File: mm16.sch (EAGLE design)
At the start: 57 parts, among them IC101 ATMEGA32-PU, IC102 DS1337, IC103 MAX483CPA, IC201 LTV847, IC202 LTV847, IC203 LTV847, IC204 LTV847, Q1 32,768kHz

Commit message: Werte im Schema und Bohrungen im Layout hinzugefügt
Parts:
- C1, C101, C102, C103: value 10nF -> 100nF
- R201, R202, R203, R204, R205, R206, R207, R208, R209, R210, R211, R212, R213, R214, R215, R216: value (none) -> 220kΩ
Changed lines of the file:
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@@
 <part name="D207" library="diode" deviceset="1N4148" device="-V"/>
 <part name="D208" library="diode" deviceset="1N4148" device="-V"/>
-<part name="R201" library="passiv" deviceset="R_" device="0204/2V"/>
-<part name="R202" library="passiv" deviceset="R_" device="0204/2V"/>
-<part name="R203" library="passiv" deviceset="R_" device="0204/2V"/>
-<part name="R204" library="passiv" deviceset="R_" device="0204/2V"/>
-<part name="R205" library="passiv" deviceset="R_" device="0204/2V"/>
-<part name="R206" library="passiv" deviceset="R_" device="0204/2V"/>
-<part name="R207" library="passiv" deviceset="R_" device="0204/2V"/>
-<part name="R208" library="passiv" deviceset="R_" device="0204/2V"/>
+<part name="R201" library="passiv" deviceset="R_" device="0204/2V" value="220kΩ"/>
+<part name="R202" library="passiv" deviceset="R_" device="0204/2V" value="220kΩ"/>
+<part name="R203" library="passiv" deviceset="R_" device="0204/2V" value="220kΩ"/>
+<part name="R204" library="passiv" deviceset="R_" device="0204/2V" value="220kΩ"/>
+<part name="R205" library="passiv" deviceset="R_" device="0204/2V" value="220kΩ"/>
+<part name="R206" library="passiv" deviceset="R_" device="0204/2V" value="220kΩ"/>
+<part name="R207" library="passiv" deviceset="R_" device="0204/2V" value="220kΩ"/>
+<part name="R208" library="passiv" deviceset="R_" device="0204/2V" value="220kΩ"/>
 <part name="GND1" library="versorgung" deviceset="GND" device=""/>
 <part name="GND2" library="versorgung" deviceset="GND" device=""/>
@@
 <part name="D215" library="diode" deviceset="1N4148" device="-V"/>
 <part name="D216" library="diode" deviceset="1N4148" device="-V"/>
-<part name="R209" library="passiv" deviceset="R_" device="0204/2V"/>
-<part name="R210" library="passiv" deviceset="R_" device="0204/2V"/>
-<part name="R211" library="passiv" deviceset="R_" device="0204/2V"/>
-<part name="R212" library="passiv" deviceset="R_" device="0204/2V"/>
-<part name="R213" library="passiv" deviceset="R_" device="0204/2V"/>
-<part name="R214" library="passiv" deviceset="R_" device="0204/2V"/>
-<part name="R215" library="passiv" deviceset="R_" device="0204/2V"/>
-<part name="R216" library="passiv" deviceset="R_" device="0204/2V"/>
+<part name="R209" library="passiv" deviceset="R_" device="0204/2V" value="220kΩ"/>
+<part name="R210" library="passiv" deviceset="R_" device="0204/2V" value="220kΩ"/>
+<part name="R211" library="passiv" deviceset="R_" device="0204/2V" value="220kΩ"/>
+<part name="R212" library="passiv" deviceset="R_" device="0204/2V" value="220kΩ"/>
+<part name="R213" library="passiv" deviceset="R_" device="0204/2V" value="220kΩ"/>
+<part name="R214" library="passiv" deviceset="R_" device="0204/2V" value="220kΩ"/>
+<part name="R215" library="passiv" deviceset="R_" device="0204/2V" value="220kΩ"/>
+<part name="R216" library="passiv" deviceset="R_" device="0204/2V" value="220kΩ"/>
 <part name="GND17" library="versorgung" deviceset="GND" device=""/>
 <part name="GND18" library="versorgung" deviceset="GND" device=""/>
@@
 <part name="GND26" library="versorgung" deviceset="GND" device=""/>
 <part name="P+3" library="versorgung" deviceset="+5V" device=""/>
-<part name="C101" library="passiv" deviceset="C_" device="025-025X050" value="10nF"/>
-<part name="C102" library="passiv" deviceset="C_" device="025-025X050" value="10nF"/>
+<part name="C101" library="passiv" deviceset="C_" device="025-025X050" value="100nF"/>
+<part name="C102" library="passiv" deviceset="C_" device="025-025X050" value="100nF"/>
 <part name="GND35" library="versorgung" deviceset="GND" device=""/>
 <part name="GND36" library="versorgung" deviceset="GND" device=""/>
@@
 <part name="P+4" library="versorgung" deviceset="+5V" device=""/>
 <part name="P+5" library="versorgung" deviceset="+5V" device=""/>
-<part name="C103" library="passiv" deviceset="C_" device="025-025X050" value="10nF"/>
+<part name="C103" library="passiv" deviceset="C_" device="025-025X050" value="100nF"/>
 <part name="P+10" library="versorgung" deviceset="+5V" device=""/>
 <part name="P+11" library="versorgung" deviceset="+5V" device=""/>
@@
 <part name="IC102" library="ic-controller" deviceset="DS1337" device=""/>
 <part name="Q1" library="passiv" deviceset="Q_" device="TC38H" value="32,768kHz"/>
-<part name="C1" library="passiv" deviceset="C_" device="025-025X050" value="10nF"/>
+<part name="C1" library="passiv" deviceset="C_" device="025-025X050" value="100nF"/>
 <part name="GND45" library="versorgung" deviceset="GND" device=""/>
 <part name="GND46" library="versorgung" deviceset="GND" device=""/>

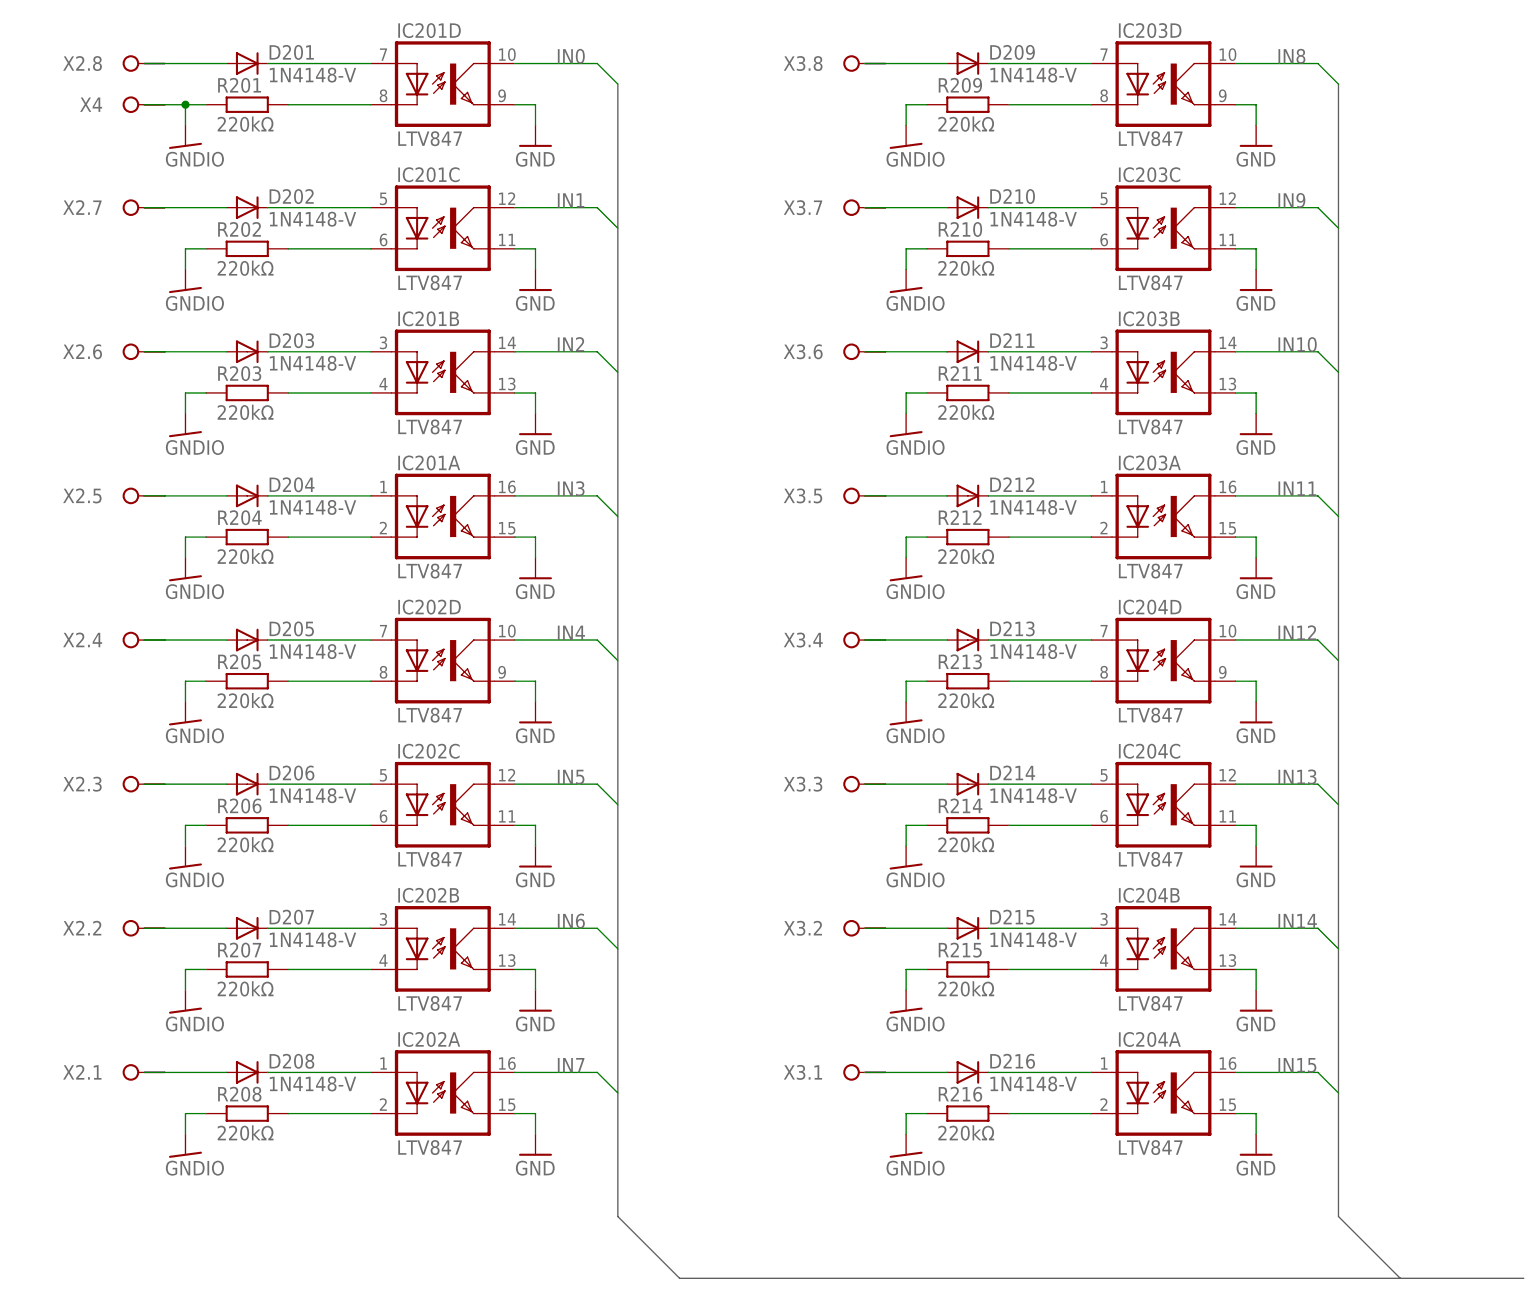
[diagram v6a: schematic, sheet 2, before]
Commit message: Anschlussklemmen ausgetauscht
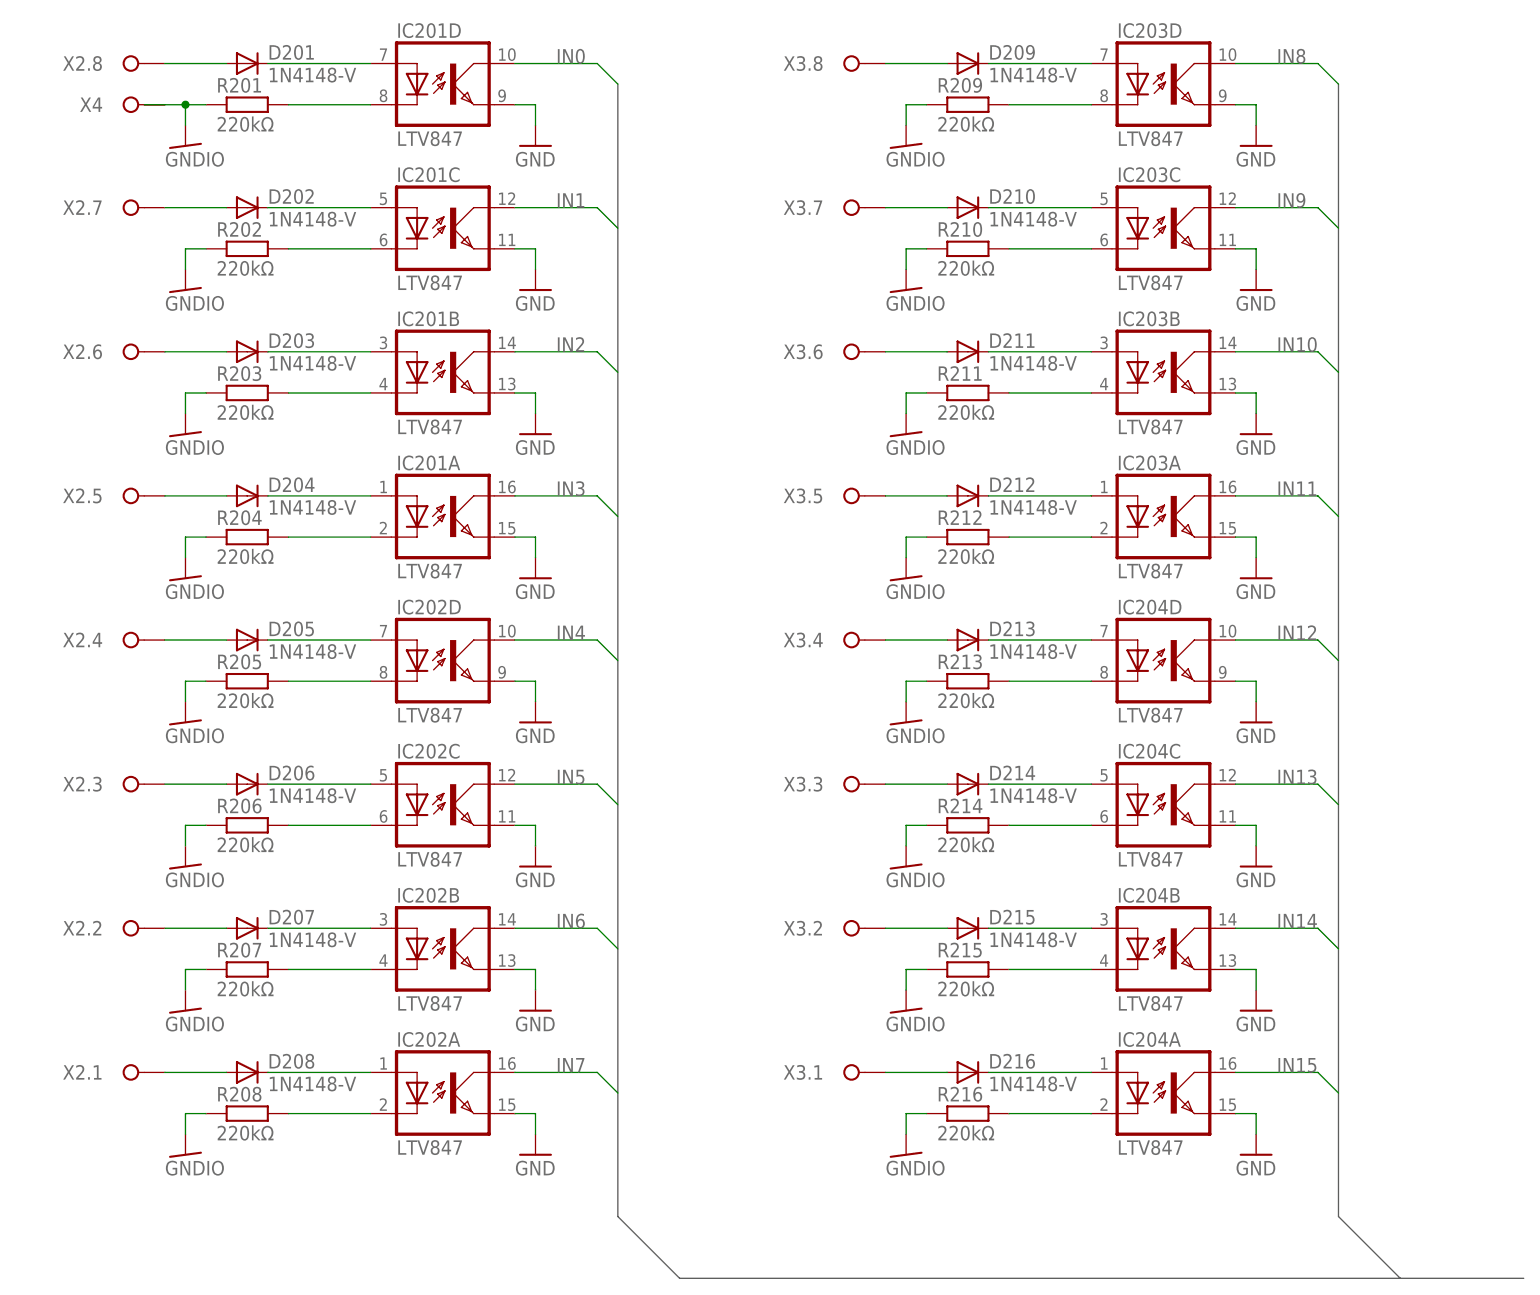
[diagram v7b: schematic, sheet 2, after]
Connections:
- net N$17: no longer X5.1.B
- net N$18: no longer X5.2.B
- net N$19: no longer X6.2.B
- net N$20: no longer X6.1.B
- net N$50: no longer X2.5.B
- net N$52: no longer X2.6.B
- net N$55: no longer X2.7.B
- net N$57: no longer X2.8.B
- net N$65: no longer X2.4.B
- net N$67: no longer X2.3.B
- net N$69: no longer X2.2.B
- net N$71: no longer X2.1.B
- net N$73: no longer X3.1.B
- net N$77: no longer X3.2.B
- net N$79: no longer X3.3.B
- net N$81: no longer X3.4.B
- net N$83: no longer X3.5.B
- net N$85: no longer X3.6.B
- net N$86: no longer X3.8.B
- net N$88: no longer X3.7.B

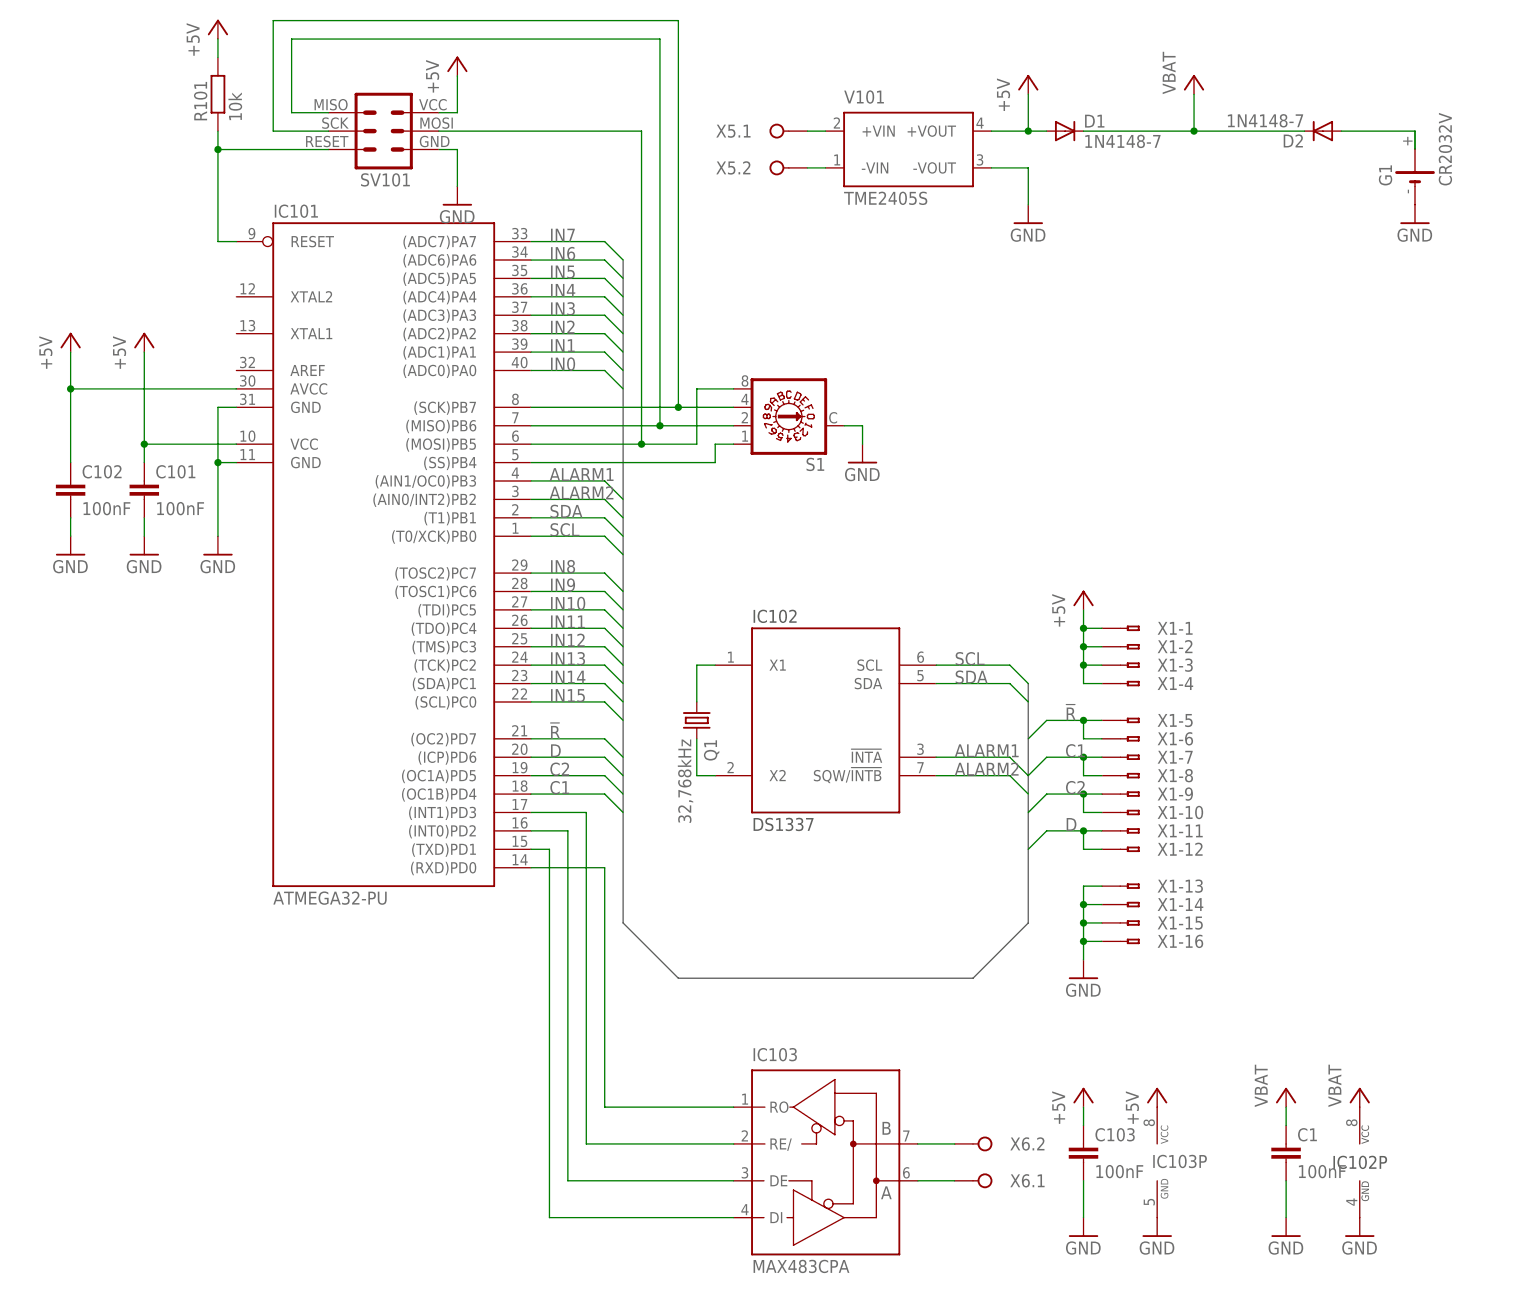
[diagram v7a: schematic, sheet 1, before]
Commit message: Optionaler Abschlusswiderstand eingefügt
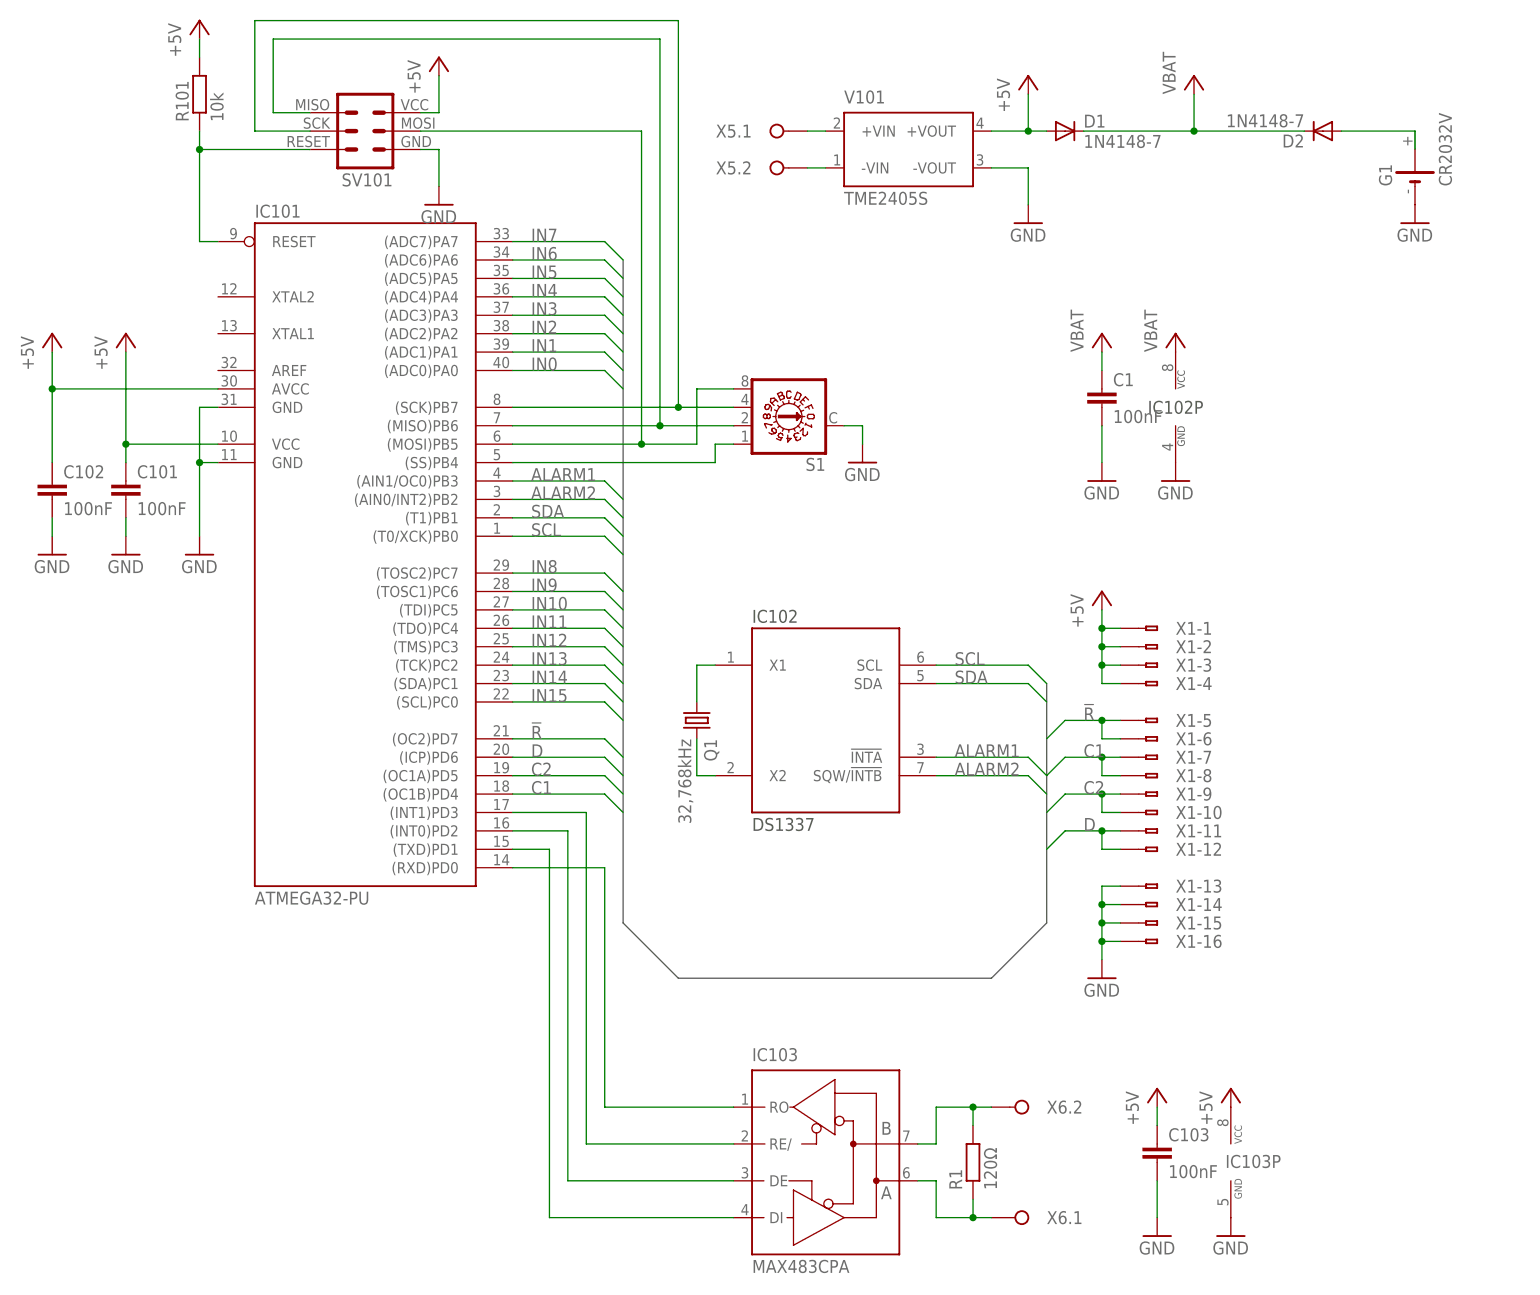
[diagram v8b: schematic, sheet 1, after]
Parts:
- added R1: 120Ω, passiv:R_0204/2V
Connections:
- removed net N$19: IC103G$1.B, X6.2.A
- new net N$22: IC103G$1.B, R1.2, X6.2.A
- net N$20: now also R1.1
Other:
- moved on the sheet: C1, C101, C102, C103, IC101, IC102P, IC103P, R101, SV101, X1-1, X1-10, X1-11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
